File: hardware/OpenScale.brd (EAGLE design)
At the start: 54.6 x 40.6 mm, 64 parts, among them Q1 200mA/50V, Q2 200mA/50V, Q3 MMBT4403, U1 HX711, U3 TMP102, U4 ATMEGA328P_TQFP, U6 FT231X, Y2 16MHZ

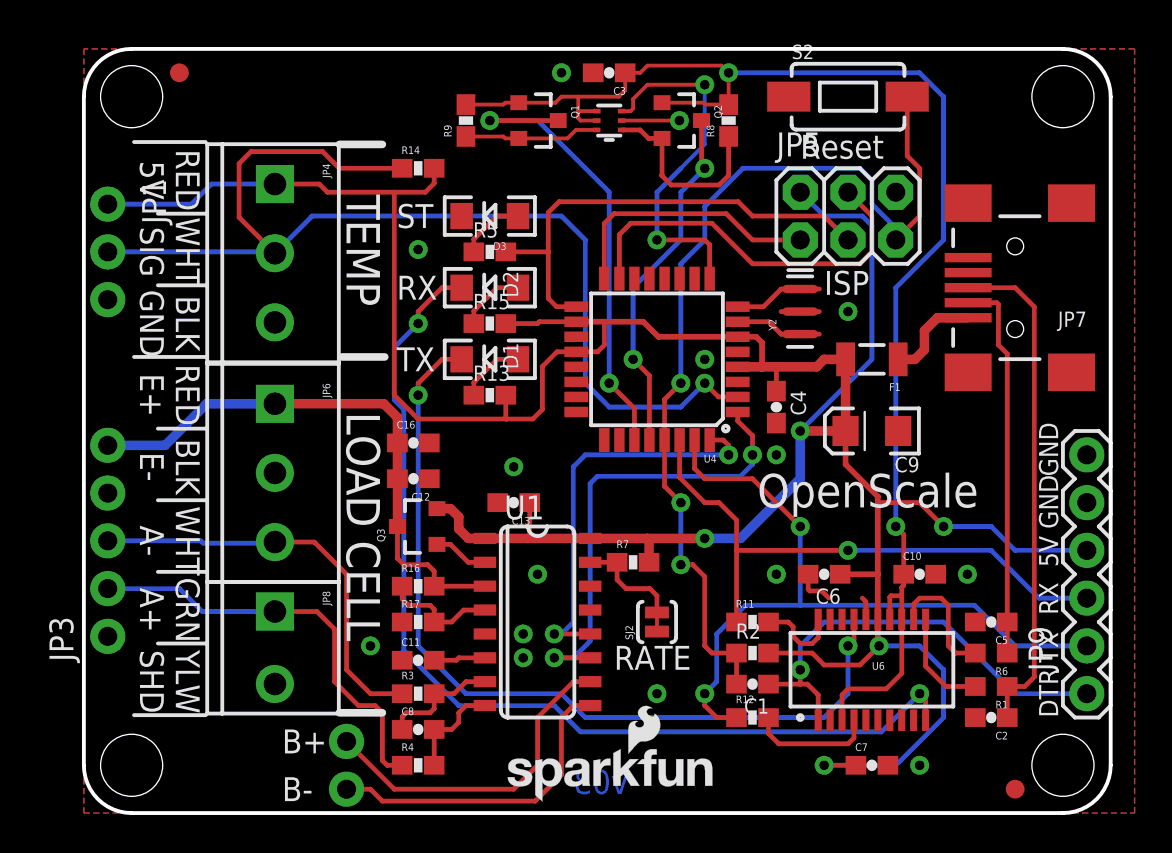
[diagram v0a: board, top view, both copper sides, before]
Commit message: Fix screw terminal spacing. Small firmware changes.
Footprint error on the screw terminals that prevented them from being
linked together (spaced too far apart). Should be fixed now but needs
double checking.
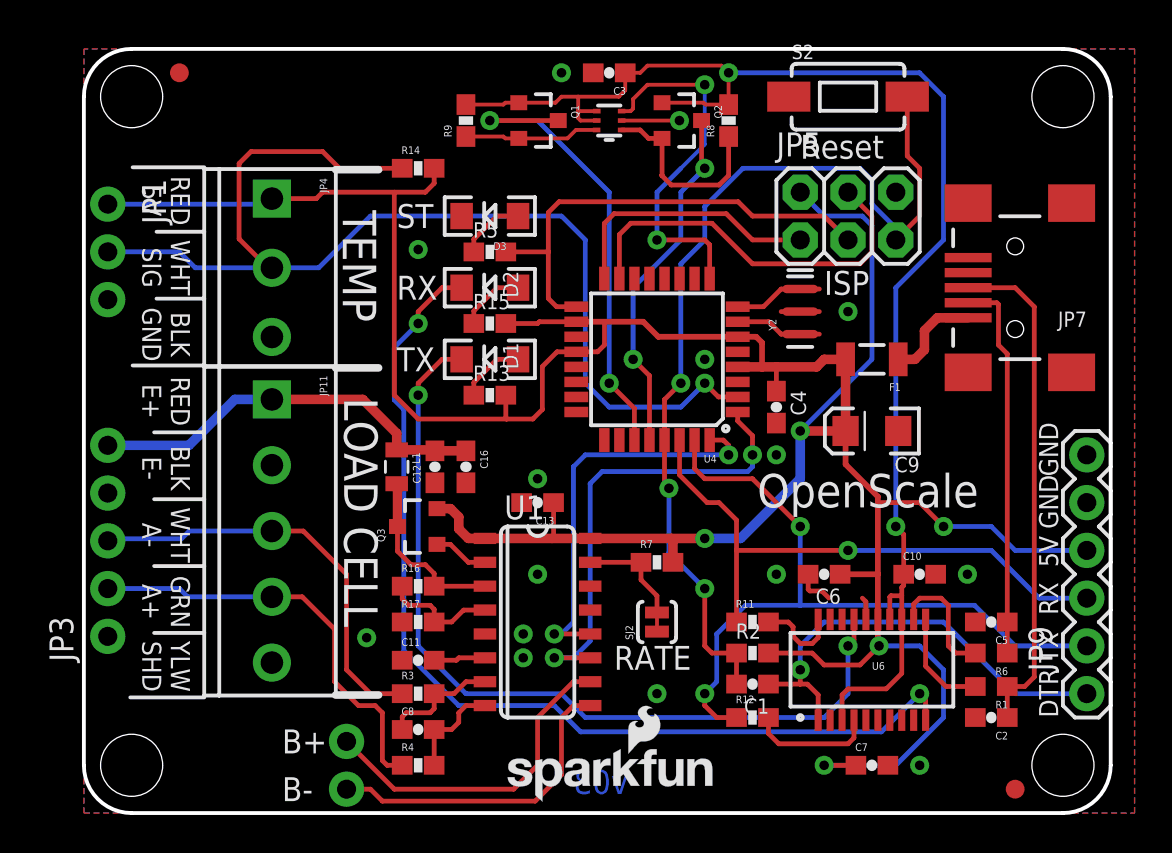
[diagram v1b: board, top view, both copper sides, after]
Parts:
- removed JP6: (no value), SparkFun-Connectors:SCREWTERMINAL-3.5MM-3_LOCK.007S
- removed JP8: (no value), SparkFun-Connectors:SCREWTERMINAL-3.5MM-2_LOCK
- added JP11: (no value), SparkFun-Connectors:SCREWTERMINAL-3.5MM-5
- added L1: 3.3uH, SparkFun-Passives:0805
- SJ2: value (none) -> JUMPER-PAD-2-NC_BY_TRACE
- moved C16 3.07 mm to (20.3, 18.4), turned to 270 degrees
- moved C12 1.31 mm to (18.7, 18.4), turned to 90 degrees
- moved C13 1.27 mm to (24.1, 16.5)
- moved R7 1.27 mm to (30.5, 13.3)
- moved JP4 0.79 mm to (10.0, 32.5)
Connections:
- new net N$15: L1.2, Q3.3, R16.2, U1.3
- net A+: now also JP11.4; no longer JP8.1
- net A-: now also JP11.3; no longer JP6.3
- net AVDD: now also JP11.1, L1.1; no longer JP6.1, Q3.3, R16.2, U1.3
- net GND: now also JP11.2, JP11.5; no longer JP6.2, JP8.2
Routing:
- net N$15: track 0.00 -> 9.42 mm
- net AVDD: track 29.9 -> 21.7 mm
- net TEMP_DAT: track 58.7 -> 60.2 mm

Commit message: Value Additions to .brd and .sch for 3D Model
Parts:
- JP11: value (none) -> SCREWTERMINAL-5
- JP4: value Screw -> SCREWTERMINAL-3
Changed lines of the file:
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@@
 <?xml version="1.0" encoding="utf-8"?>
 <!DOCTYPE eagle SYSTEM "eagle.dtd">
-<eagle version="7.1.0">
+<eagle version="7.2.0">
 <drawing>
 <settings>
@@
 </element>
 <element name="LOGO3" library="SparkFun-Aesthetics" package="SFE_LOGO_FLAME_STOP_.1" value="SFE_LOGO_FLAME.1_STOP" x="46.482" y="35.179"/>
-<element name="JP4" library="SparkFun-Connectors" package="SCREWTERMINAL-3.5MM-3_LOCK.007S" value="Screw" x="10" y="32.5" rot="R270">
+<element name="JP4" library="SparkFun-Connectors" package="SCREWTERMINAL-3.5MM-3_LOCK.007S" value="SCREWTERMINAL-3" x="10" y="32.5" rot="R270">
 <attribute name="PROD_ID" value="CONN-08288" x="10" y="32.5" size="1.778" layer="27" rot="R270" display="off"/>
 </element>
 <element name="JP3" library="SparkFun-Connectors" package="1X05_NO_SILK" value="" x="1.27" y="9.398" rot="R90"/>
-<element name="JP11" library="SparkFun-Connectors" package="SCREWTERMINAL-3.5MM-5" value="" x="10" y="22" rot="R270">
+<element name="JP11" library="SparkFun-Connectors" package="SCREWTERMINAL-3.5MM-5" value="SCREWTERMINAL-5" x="10" y="22" rot="R270">
 <attribute name="PROD_ID" value="Combine 8288+8399" x="10" y="22" size="1.778" layer="27" rot="R270" display="off"/>
 </element>
